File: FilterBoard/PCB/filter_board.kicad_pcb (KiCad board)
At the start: 2 copper layers, 123 x 55 mm, 23 parts, among them J2 Banana Terminals

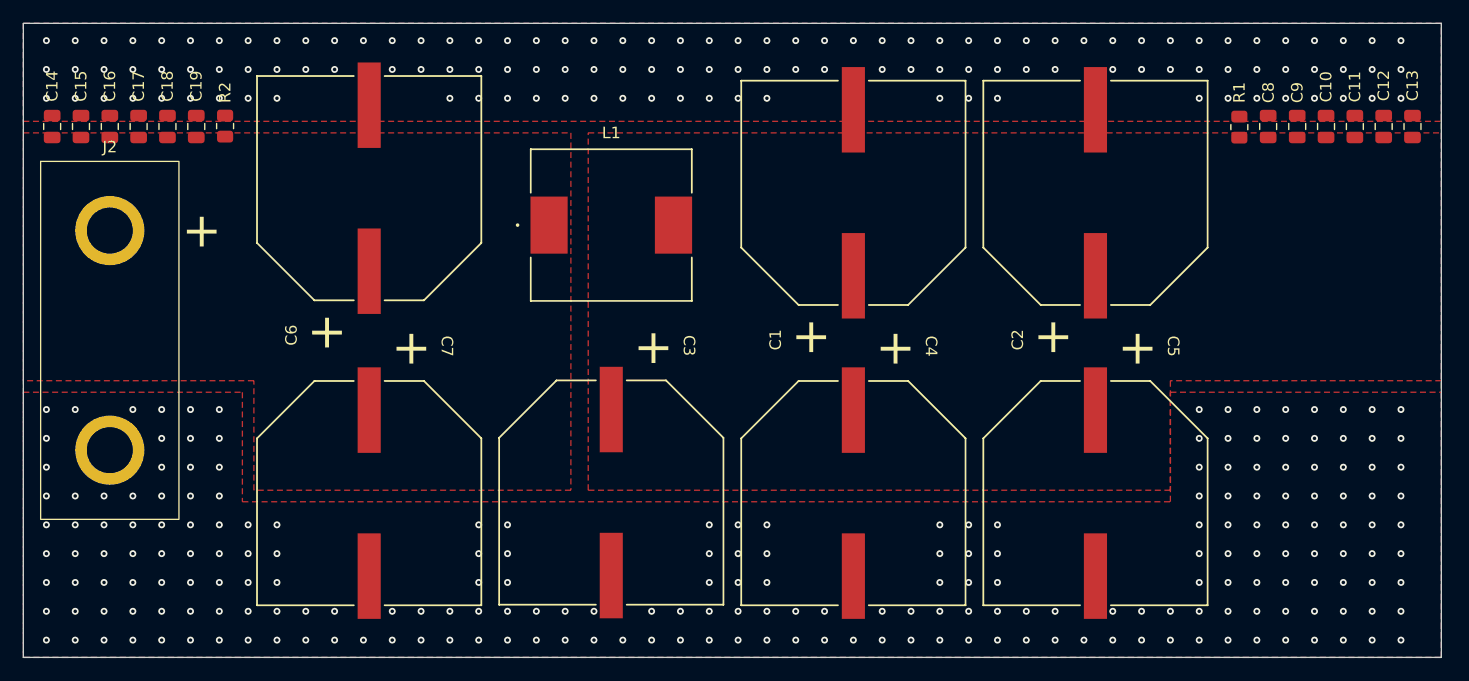
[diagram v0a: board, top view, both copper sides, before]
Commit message: Filter board layout tweaks
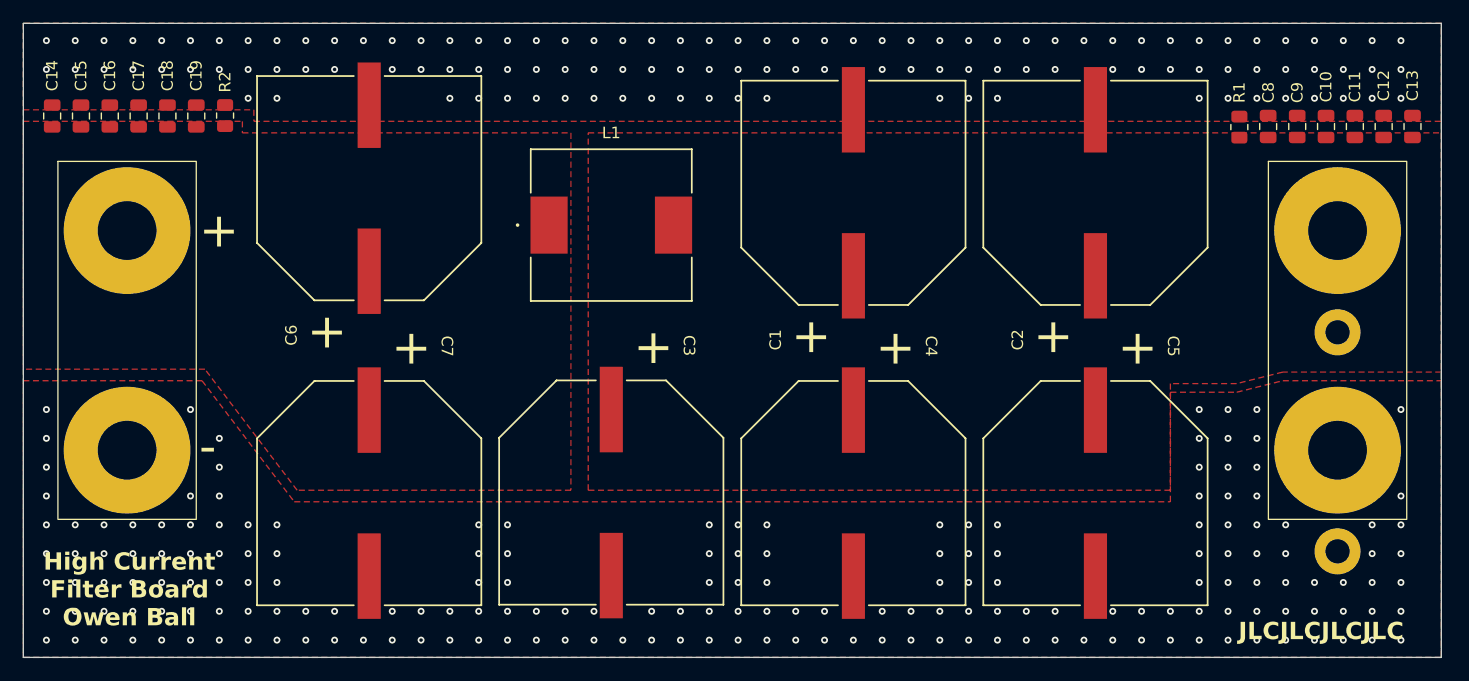
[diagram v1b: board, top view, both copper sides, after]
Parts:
- added J1: ~, FilterBoardLib:Banana_Terminals, F.Cu at (209.0, 118.0)
- added J3: Conn_01x01_Pin, FilterBoardLib:Wire_Pad, F.Cu at (209.0, 126.8)
- added J4: Conn_01x01_Pin, FilterBoardLib:Wire_Pad, F.Cu at (209.0, 145.8)
- moved J2 1.50 mm to (104.0, 118.0)
- moved C14 0.91 mm to (97.5, 108.0)
- moved C15 0.91 mm to (100.0, 108.0)
- moved C16 0.91 mm to (102.5, 108.0)
- moved C17 0.91 mm to (105.0, 108.0)
- moved C18 0.91 mm to (107.5, 108.0)
- moved C19 0.91 mm to (110.0, 108.0)
- moved R2 0.91 mm to (112.5, 108.0)
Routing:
- net GND: vias 345 -> 304
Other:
- board text added: "High Current Filter Board Owen Ball"
- board text added: "JLCJLCJLCJLC"
